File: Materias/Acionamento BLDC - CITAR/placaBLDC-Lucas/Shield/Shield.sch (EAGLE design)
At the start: 37 parts, among them IC1 LMC6484, U1 DRV8811_PWP_28, U2 52207-1185

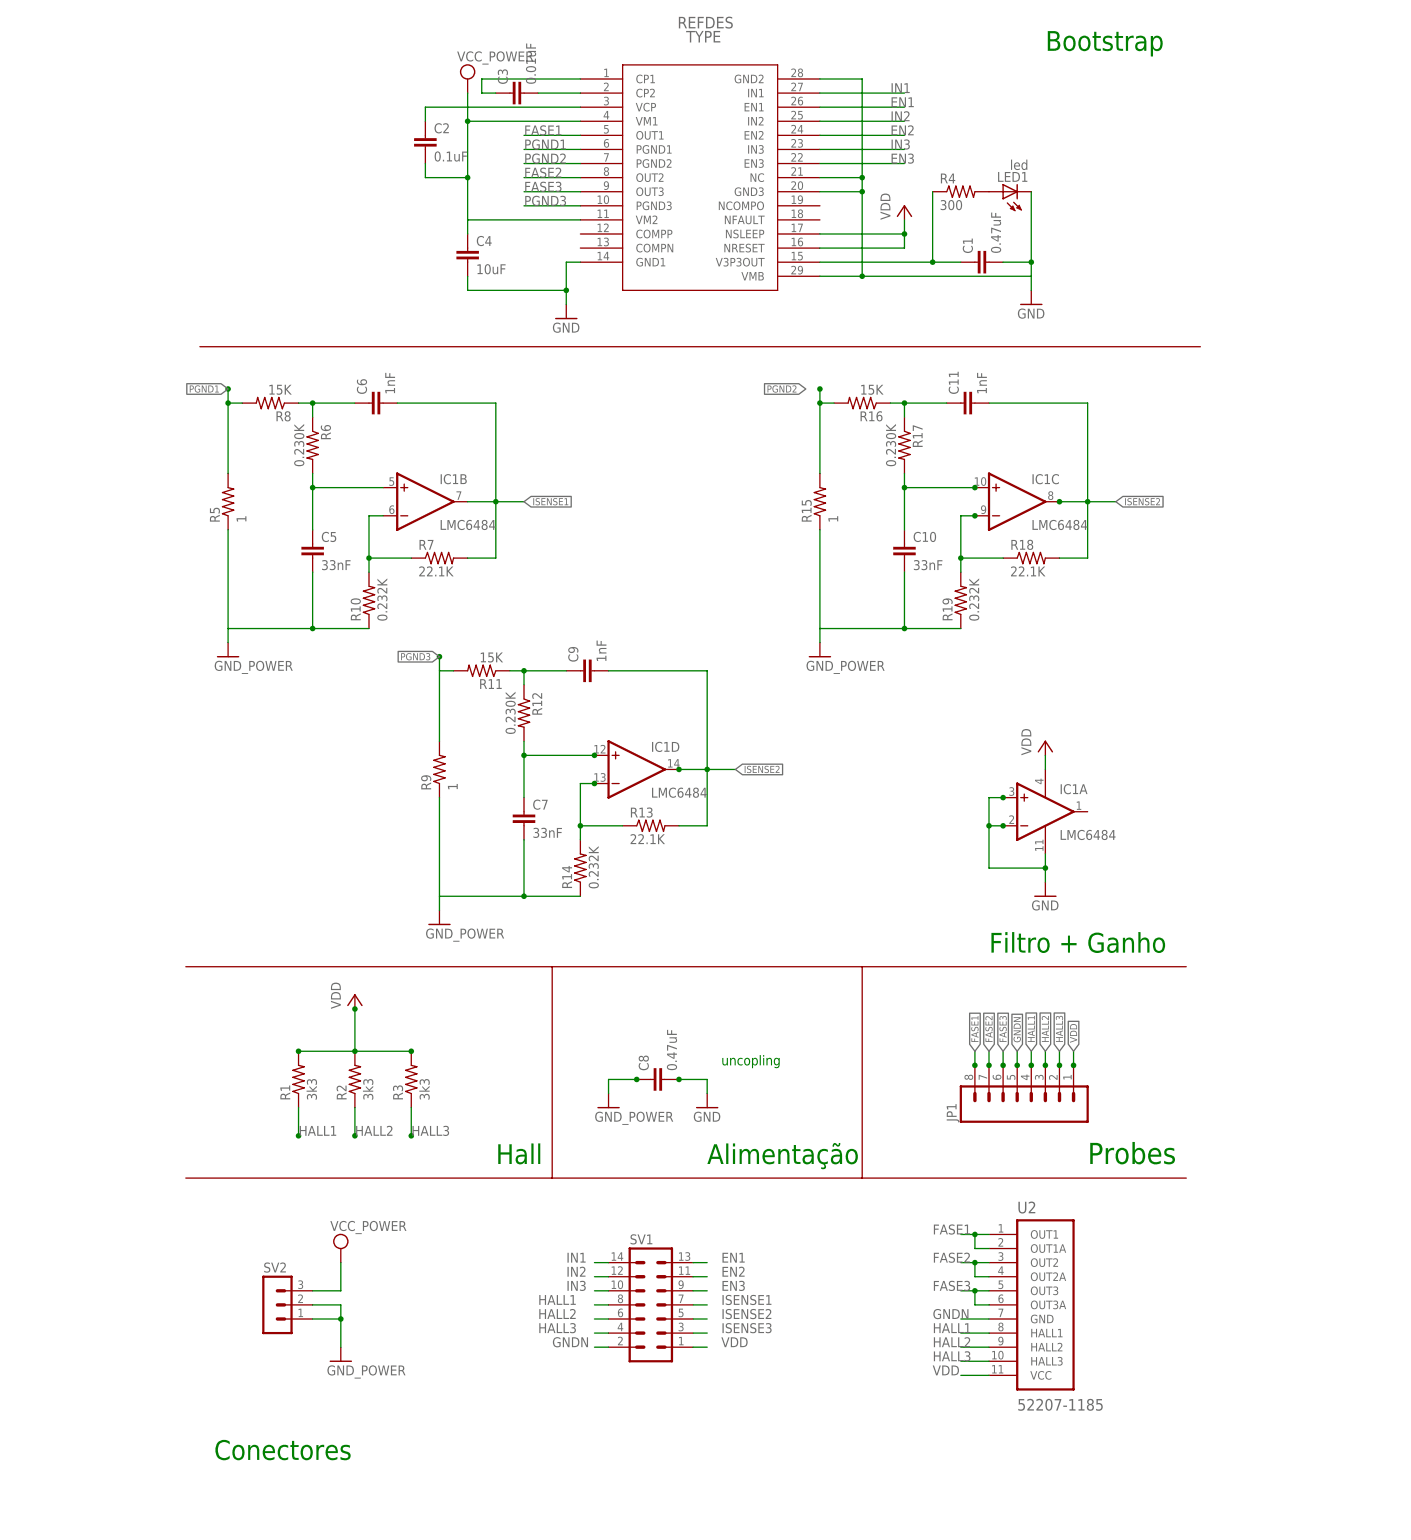
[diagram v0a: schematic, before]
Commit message: adicionado BOM e PCB lucas
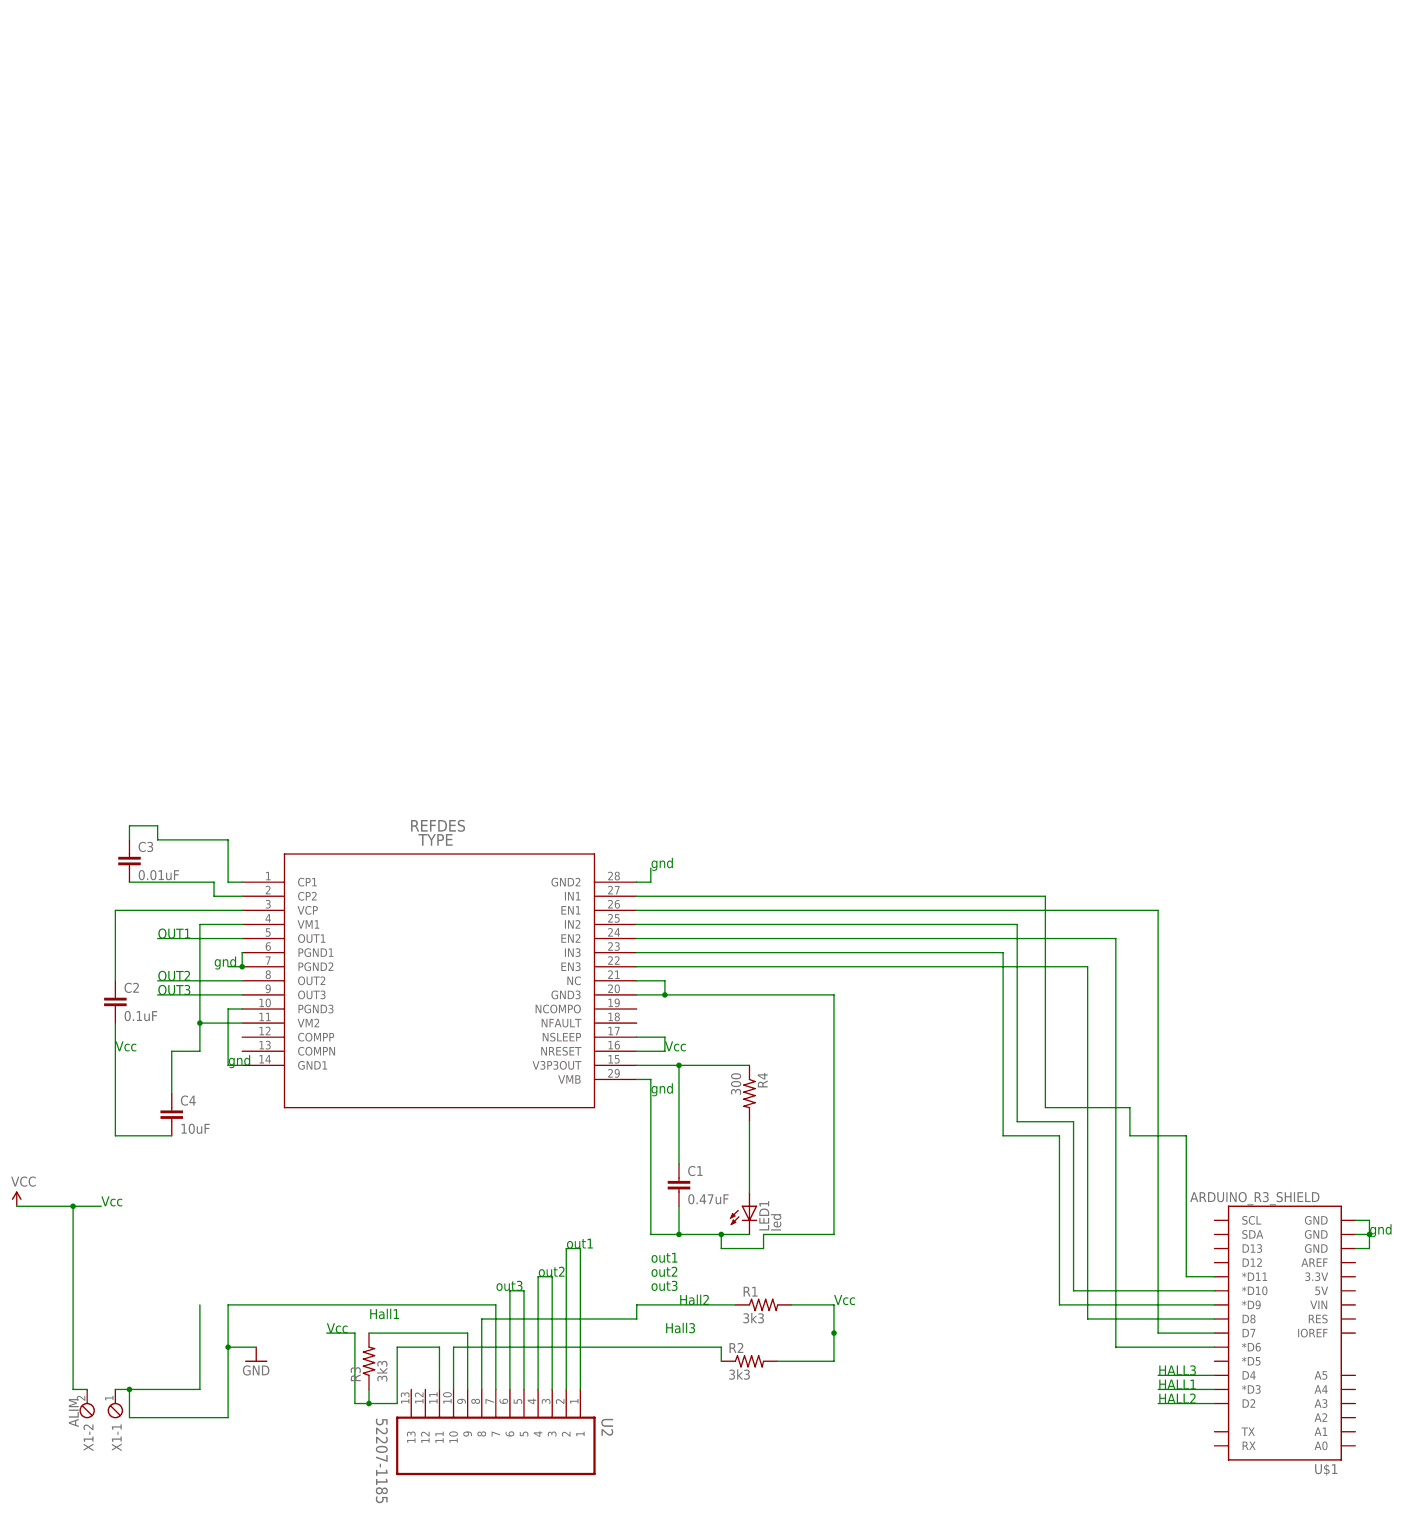
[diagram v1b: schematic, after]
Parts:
- removed C10, C5, C7: 33nF, rcl:C-EUC1206
- removed C11, C6, C9: 1nF, rcl:C-EUC1206
- removed C8: 0.47uF, rcl:C-EUC1206
- removed IC1: LMC6484, lmc6484:LMC6484
- removed JP1: (no value), SparkFun-Connectors:M08
- removed R10, R14, R19: 0.232K, adafruit:R-US_R1206
- removed R11, R16, R8: 15K, adafruit:R-US_R1206
- removed R12, R17, R6: 0.230K, adafruit:R-US_R1206
- removed R13, R18, R7: 22.1K, adafruit:R-US_R1206
- removed R15, R5, R9: 1, adafruit:R-US_R1206
- removed SV1: (no value), con-lstb:MA07-2
- removed SV2: (no value), con-lstb:MA03-1
- added U$1: ARDUINO_R3_SHIELD, SparkFun-Boards:ARDUINO_R3_SHIELD
- added X1: ALIM, con-phoenix-254:MPT2
- C1, C3: device rcl:C-EUC1206 -> rcl:C-EU025-025X050
- C2: device rcl:C-EUC1206 -> rcl:C-EU102-043X133
- C4: device rcl:C-EUC1206 -> rcl:C-EU025-050X050
- LED1: device adafruit:LEDCHIPLED_1206 -> adafruit:LED3MM
- R1, R2, R3, R4: device adafruit:R-US_R1206 -> adafruit:R-US_0207/10
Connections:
- removed net EN1: SV1.13, U1.EN1
- removed net EN2: SV1.11, U1.EN2
- removed net EN3: SV1.9, U1.EN3
- removed net FASE1: JP1.8, U1.OUT1, U2.OUT1, U2.OUT1A
- removed net FASE2: JP1.7, U1.OUT2, U2.OUT2, U2.OUT2A
- removed net FASE3: JP1.6, U1.OUT3, U2.OUT3, U2.OUT3A
- removed net GNDN: C1.2, C4.2, C8.2, JP1.5, LED1.C, SV1.2, SV2.1, SV2.2, U1.GND1, U1.GND2, U1.GND3, U1.NC, U1.VMB, U2.GND
- removed net GND_POWER: C8.1
- removed net IN1: SV1.14, U1.IN1
- removed net IN2: SV1.12, U1.IN2
- removed net IN3: SV1.10, U1.IN3
- removed net ISENSE1: C6.2, IC1B.OUT, R7.2, SV1.7
- removed net ISENSE2: C11.2, IC1C.OUT, R18.2, SV1.5
- removed net ISENSE3: C9.2, IC1D.OUT, R13.2, SV1.3
- removed net N$12 (its old number): IC1C.-IN, R18.1, R19.2
- removed net N$2: C5.1, IC1B.+IN, R6.2
- removed net N$3: IC1B.-IN, R10.2, R7.1
- removed net PGND1: R5.2, R8.2, U1.PGND1
- removed net PGND2: R15.2, R16.2, U1.PGND2
- removed net PGND3: R11.2, R9.2, U1.PGND3
- removed net VCC_POWER: C2.2, C4.1, SV2.3, U1.VM1, U1.VM2
- removed net VDD: IC1P.V+, JP1.1, R1.2, R2.2, R3.2, SV1.1, U1.NRESET, U1.NSLEEP, U2.VCC
- new net N$15: C4.1, U1.VM1, U1.VM2
- new net OUT1: U1.OUT1, U2.1, U2.2
- new net OUT2: U1.OUT2, U2.3, U2.4
- new net OUT3: U1.OUT3, U2.5, U2.6
- new net VCC: C2.2, C4.2, R1.2, R2.2, R3.1, U1.NRESET, U1.NSLEEP, U2.11, X1-2.1
- net GND: now also C1.2, LED1.C, U$1.GND@0, U$1.GND@1, U$1.GND@2, U1.GND1, U1.GND2, U1.GND3, U1.NC, U1.PGND1, U1.PGND2, U1.PGND3, U1.VMB, U2.7, X1-1.1; no longer C10.2, C5.2, C7.2, IC1A.+IN, IC1A.-IN, IC1P.V-, R10.1, R14.1, R15.1, R19.1, R5.1, R9.1
- net HALL1: now also R3.2, U$1.*D3, U2.9; no longer JP1.4, R1.1, SV1.8, U2.HALL1
- net HALL2: now also R1.1, U$1.D2, U2.8; no longer JP1.3, R2.1, SV1.6, U2.HALL2
- net HALL3: now also R2.1, U$1.D4, U2.10; no longer JP1.2, R3.1, SV1.4, U2.HALL3
- net N$4: now also U$1.*D11, U1.IN1; no longer C6.1, R6.1, R8.1
- net N$5: now also U$1.D7, U1.EN1; no longer C9.1, R11.1, R12.1
- net N$6: now also U$1.*D6, U1.EN2; no longer C7.1, IC1D.+IN, R12.2
- net N$7: now also U$1.*D10, U1.IN2; no longer IC1D.-IN, R13.1, R14.2
- net N$8: now also U$1.*D9, U1.IN3; no longer C11.1, R16.1, R17.1
- net N$9: now also U$1.D8, U1.EN3; no longer C10.1, IC1C.+IN, R17.2
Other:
- note added: "HALL1"
- note added: "HALL2"
- note added: "HALL3"
- note added: "Hall1"
- note added: "Hall2"
- note added: "Hall3"
- note added: "OUT1"
- note added: "OUT2"
- note added: "OUT3"
- note added: "Vcc"
- note added: "gnd"
- note added: "out1"
- note added: "out2"
- note added: "out3"
- note removed: "Alimentação"
- note removed: "Bootstrap"
- note removed: "Conectores"
- note removed: "Filtro + Ganho"
- note removed: "Hall"
- note removed: "Probes"
- note removed: "uncopling"
- moved on the sheet: C1, C2, C3, C4, LED1, R1, R2, R3, R4
